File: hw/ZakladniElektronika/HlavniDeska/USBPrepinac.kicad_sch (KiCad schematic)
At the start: 3 parts, among them J9 Conn_01x02

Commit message: Likvidace MiniUI jako samostatné desky a výběr všech komponent
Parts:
- J9: footprint (none) -> Connector_PinHeader_2.54mm:PinHeader_1x02_P2.54mm_Vertical; JLCPCB_IGNORE (none) -> ignore
- R13: JLCPCB_CORRECTION (none) -> 0;0;0
- U?: Basic/Extended (none) -> E; LCSC (none) -> C2652459
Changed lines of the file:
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@@
+      (effects (font (size 1.27 1.27)) hide)
+    )
+    (property "Basic/Extended" "E" (at 170.18 58.42 0)
+      (effects (font (size 1.27 1.27)) hide)
+    )
+    (property "LCSC" "C2652459" (at 170.18 58.42 0)
       (effects (font (size 1.27 1.27)) hide)
     )
@@
       (effects (font (size 1.27 1.27)))
     )
-    (property "Footprint" "" (at 93.98 93.98 0)
+    (property "Footprint" "Connector_PinHeader_2.54mm:PinHeader_1x02_P2.54mm_Vertical" (at 93.98 93.98 0)
       (effects (font (size 1.27 1.27)) hide)
     )
     (property "Datasheet" "~" (at 93.98 93.98 0)
+      (effects (font (size 1.27 1.27)) hide)
+    )
+    (property "JLCPCB_IGNORE" "ignore" (at 93.98 93.98 0)
       (effects (font (size 1.27 1.27)) hide)
     )
@@
       (effects (font (size 1.27 1.27)) hide)
     )
+    (property "JLCPCB_CORRECTION" "0;0;0" (at 101.6 100.33 0)
+      (effects (font (size 1.27 1.27)) hide)
+    )

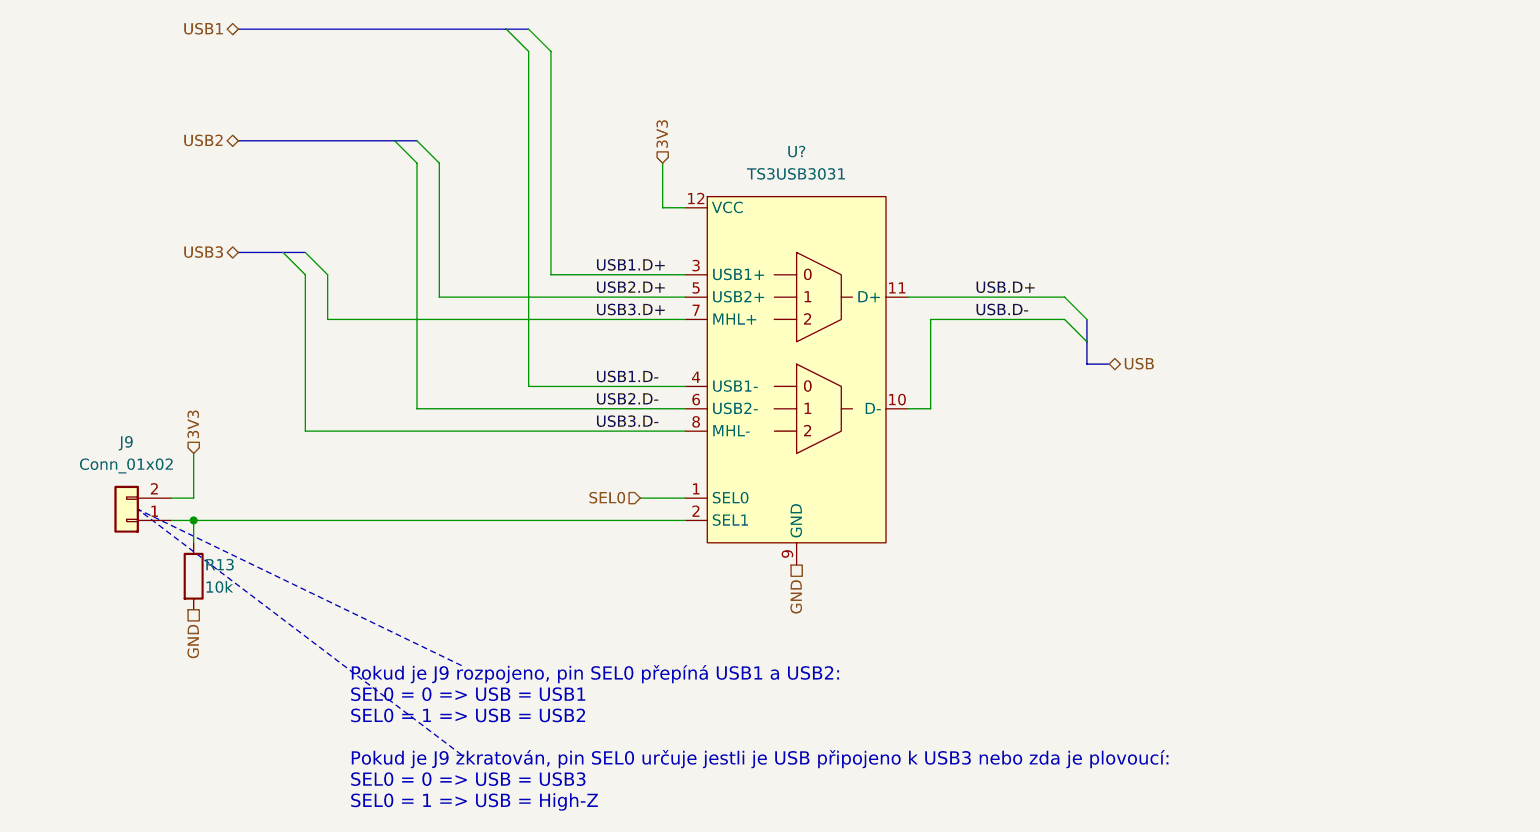
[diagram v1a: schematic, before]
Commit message: Výmněna ochrany baterie
Předchozí ochranný čip JLCPCB nemělo na skladě
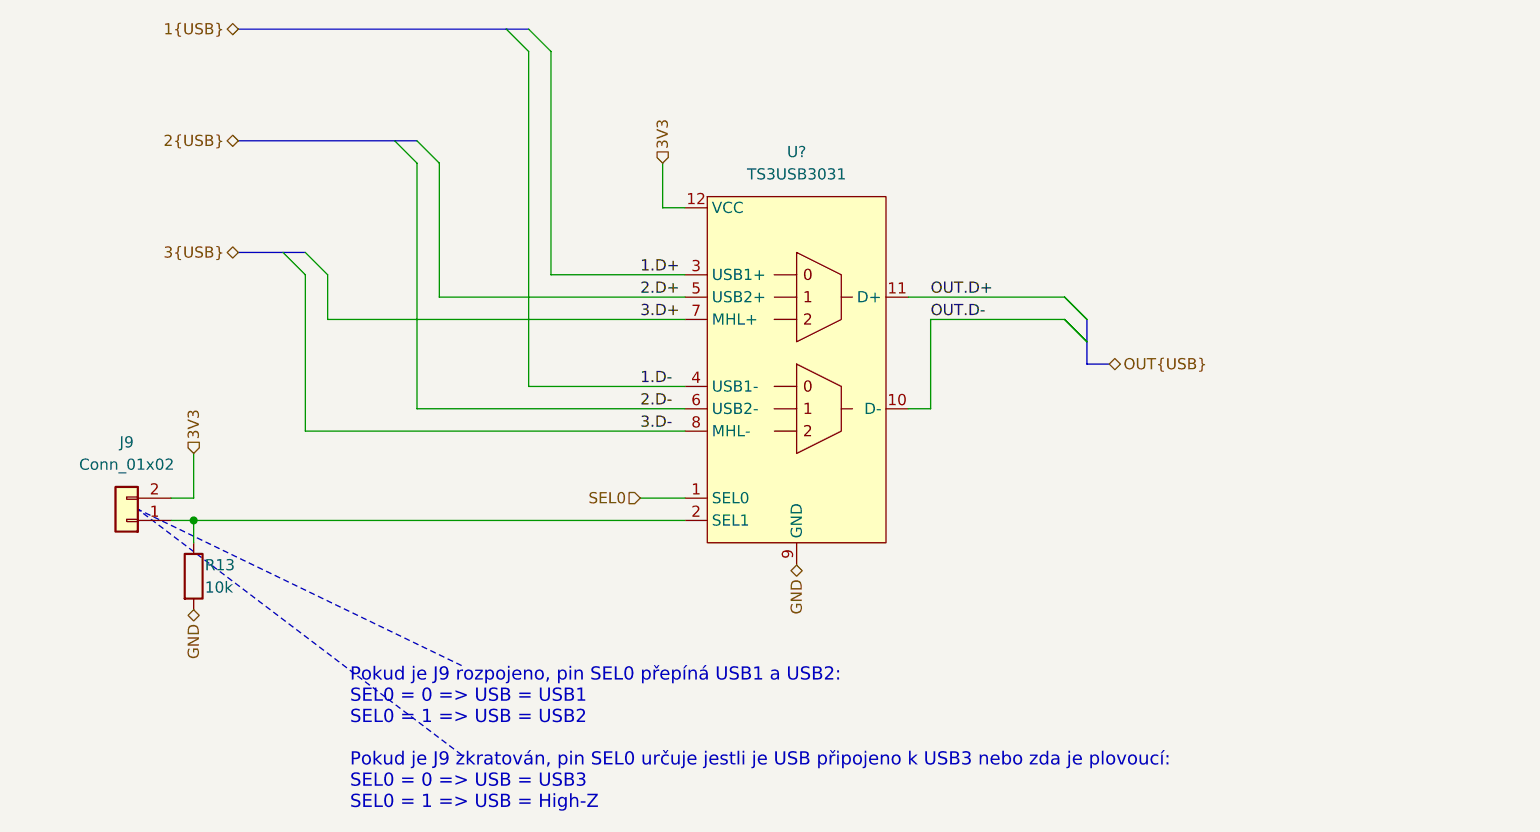
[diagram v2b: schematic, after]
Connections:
- net USB.D+ renamed OUT.D+
- net USB.D- renamed OUT.D-
- net USB1.D+ renamed 1.D+
- net USB1.D- renamed 1.D-
- net USB2.D+ renamed 2.D+
- net USB2.D- renamed 2.D-
- net USB3.D+ renamed 3.D+
- net USB3.D- renamed 3.D-
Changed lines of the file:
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@@
+    (stroke (width 0) (type default))
+  )
+  (bus_entry (at 203.2 71.12) (size -2.54 -2.54)
     (stroke (width 0) (type default))
   )
@@
   )
   (bus_entry (at 139.7 40.64) (size -2.54 -2.54)
+    (stroke (width 0) (type default))
+  )
+  (bus_entry (at 203.2 73.66) (size -2.54 -2.54)
     (stroke (width 0) (type default))
   )
@@
     (effects (font (size 1.5 1.5)) (justify left bottom))
   )
-  (label "USB1.D-" (at 147.32 78.74 0) (fields_autoplaced)
+  (label "1.D-" (at 152.4 78.74 0) (fields_autoplaced)
     (effects (font (size 1.27 1.27)) (justify left bottom))
   )
-  (label "USB3.D-" (at 147.32 83.82 0) (fields_autoplaced)
+  (label "3.D-" (at 152.4 83.82 0) (fields_autoplaced)
     (effects (font (size 1.27 1.27)) (justify left bottom))
   )
-  (label "USB2.D-" (at 147.32 81.28 0) (fields_autoplaced)
+  (label "OUT.D-" (at 185.42 71.12 0) (fields_autoplaced)
     (effects (font (size 1.27 1.27)) (justify left bottom))
   )
-  (label "USB1.D+" (at 147.32 66.04 0) (fields_autoplaced)
+  (label "OUT.D+" (at 185.42 68.58 0) (fields_autoplaced)
     (effects (font (size 1.27 1.27)) (justify left bottom))
   )
-  (label "USB3.D+" (at 147.32 71.12 0) (fields_autoplaced)
+  (label "2.D-" (at 152.4 81.28 0) (fields_autoplaced)
     (effects (font (size 1.27 1.27)) (justify left bottom))
   )
-  (label "USB2.D+" (at 147.32 68.58 0) (fields_autoplaced)
+  (label "1.D+" (at 152.4 66.04 0) (fields_autoplaced)
     (effects (font (size 1.27 1.27)) (justify left bottom))
   )
-  (label "USB.D+" (at 190.5 68.58 0) (fields_autoplaced)
+  (label "3.D+" (at 152.4 71.12 0) (fields_autoplaced)
     (effects (font (size 1.27 1.27)) (justify left bottom))
   )
-  (label "USB.D-" (at 190.5 71.12 0) (fields_autoplaced)
+  (label "2.D+" (at 152.4 68.58 0) (fields_autoplaced)
     (effects (font (size 1.27 1.27)) (justify left bottom))
   )
-  (hierarchical_label "GND" (shape passive) (at 170.18 99.06 270) (fields_autoplaced)
+  (hierarchical_label "GND" (shape bidirectional) (at 170.18 99.06 270) (fields_autoplaced)
     (effects (font (size 1.27 1.27)) (justify right))
   )
-  (hierarchical_label "USB1" (shape bidirectional) (at 106.68 38.1 180) (fields_autoplaced)
+  (hierarchical_label "1{USB}" (shape bidirectional) (at 106.68 38.1 180) (fields_autoplaced)
     (effects (font (size 1.27 1.27)) (justify right))
   )
-  (hierarchical_label "USB" (shape bidirectional) (at 205.74 76.2 0) (fields_autoplaced)
+  (hierarchical_label "OUT{USB}" (shape bidirectional) (at 205.74 76.2 0) (fields_autoplaced)
     (effects (font (size 1.27 1.27)) (justify left))
   )
-  (hierarchical_label "GND" (shape passive) (at 101.6 104.14 270) (fields_autoplaced)
+  (hierarchical_label "GND" (shape bidirectional) (at 101.6 104.14 270) (fields_autoplaced)
     (effects (font (size 1.27 1.27)) (justify right))
   )
-  (hierarchical_label "USB3" (shape bidirectional) (at 106.68 63.5 180) (fields_autoplaced)
+  (hierarchical_label "3{USB}" (shape bidirectional) (at 106.68 63.5 180) (fields_autoplaced)
     (effects (font (size 1.27 1.27)) (justify right))
   )
@@
     (effects (font (size 1.27 1.27)) (justify left))
   )
-  (hierarchical_label "USB2" (shape bidirectional) (at 106.68 50.8 180) (fields_autoplaced)
+  (hierarchical_label "2{USB}" (shape bidirectional) (at 106.68 50.8 180) (fields_autoplaced)
     (effects (font (size 1.27 1.27)) (justify right))
   )

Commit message: KiCad V8
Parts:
- gave numbers to parts that had none: 1
- renumbered R13 to R22

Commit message: Hw wip
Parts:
- removed J9: Conn_01x02, Connector_PinHeader_2.54mm:PinHeader_1x02_P2.54mm_Vertical, symbol Connector_Generic:Conn_01x02
- removed R22: 10k, Resistor_SMD:R_0402_1005Metric, symbol Device:R
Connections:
- net GND: now also U15.2 (SEL1)
- net 3.D+: no longer names the net of U15.7 (MHL+)
- net 3.D-: no longer names the net of U15.8 (MHL-)
- no-connect marks 0 -> 2
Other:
- note added: "SEL0 = 0 => USB = USB1 SEL0 = 1 => USB = USB2"
- note removed: "Pokud je J9 rozpojeno, pin SEL0 přepíná USB1 a USB2: SEL0 = 0 => USB = USB1 SEL0 = 1 => USB = USB2 Pokud je J9 zkratován, pin SEL0 určuje jestli je USB připojeno k USB3 nebo zda je plovoucí: SEL0 = 0 => USB = USB3 SEL0 = 1 => USB = High-Z"

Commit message: Hw PCB
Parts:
- removed U15: TS3USB3031, Package_DFN_QFN:Texas_X2QFN-12_1.6x1.6mm_P0.4mm, symbol RKL-DiscreteLogic:TS3USB3031
- added C162: 10u, Capacitor_SMD:C_0603_1608Metric, symbol Device:C
- added R2: 10k, Resistor_SMD:R_0402_1005Metric, symbol Device:R
- added U2: BL1530TQFN, Package_DFN_QFN:UQFN-10_1.4x1.8mm_P0.4mm, symbol RKL-Uncategorized:BL1530TQFN
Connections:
- net 1.D+: now also U2.1 (Dp1)
- net 1.D-: now also U2.7 (Dn1)
- net 2.D+: now also U2.2 (Dp2)
- net 2.D-: now also U2.6 (Dn2)
- net GND: now also C162.2, U2.4 (GND), U2.8 (OEb)
- new net 0.D+: U2.3 (Dp)
- new net 0.D-: U2.5 (Dn)
- new net USB_SEL: R2.2, U2.10 (SEL)
- new net VUSB: C162.1, R2.1, U2.9 (VCC)
- no-connect marks 2 -> 0
